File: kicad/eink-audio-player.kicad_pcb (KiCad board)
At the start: 2 copper layers, 61 x 76.1 mm, 24 parts, among them J1 Feather 16-pin, J10 TLV MICBIAS..MIC, J2 Feather 12-pin, J4 EYESPI 1-9 (5613 JP2), J5 EYESPI 10-18 (5613 JP1), J9 TLV VIN..SPKP, SW1 Power (MSK-12C03)

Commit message: High-detail Adafruit board models, ANO thumb encoder and its stand mount
Board models are Adafruit's CAD parts on Adafruit's own Eagle boards imported
into KiCad (black mask, silkscreen, ENIG pads); kicad/3d/adafruit-hq rebuilds
them. The ANO rotary encoder (6310) sits on a new printed ano_mount past the
right end of the keys, and in the KiCad design as a reference part. Renders,
anatomy and docs regenerated.

Co-Authored-By: Claude Opus 5.5 (1M context) <noreply@anthropic.com>
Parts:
- added ANO1: ANO rotary encoder (6310), stand-mounted, reference, , B.Cu at (66.7, 172.7)

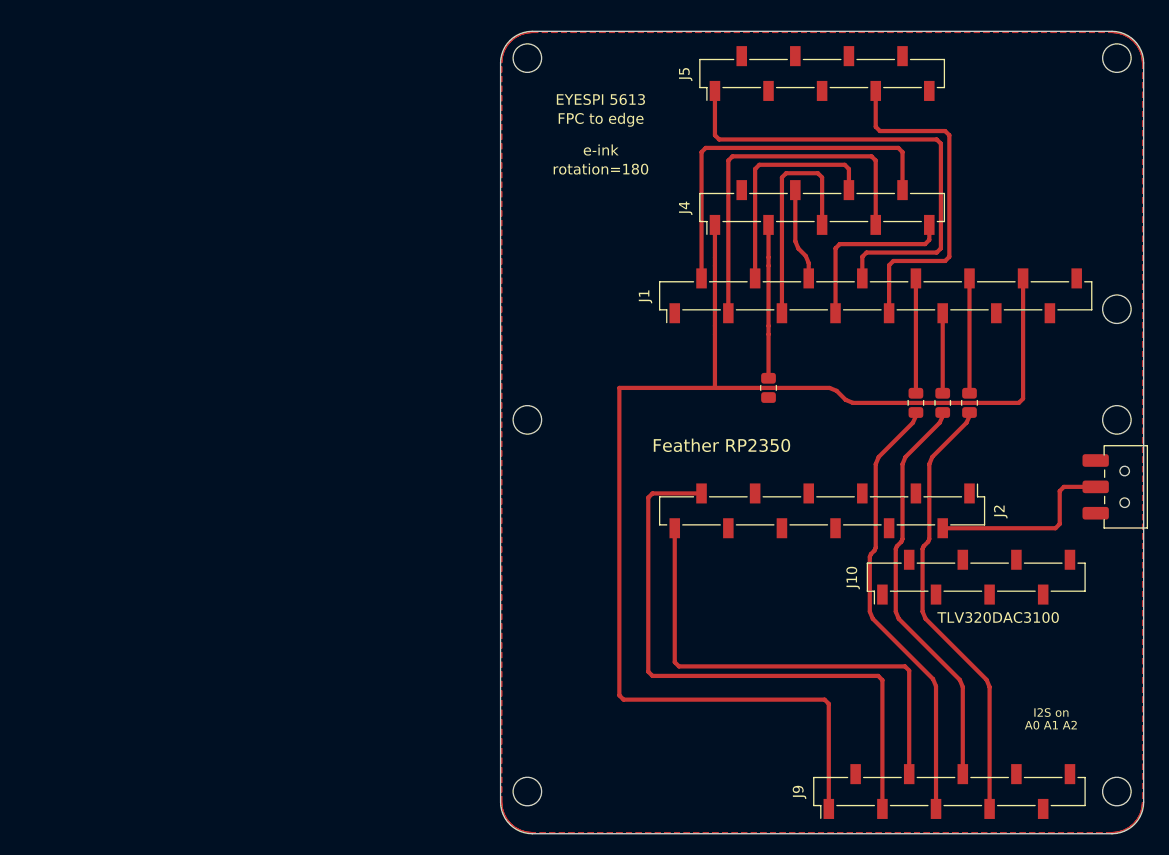
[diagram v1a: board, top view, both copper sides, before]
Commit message: Rotate the board 90 degrees to landscape (76 x 61 mm)
Drawing only; the board sits on the stand as before.

Co-Authored-By: Claude Opus 5.5 (1M context) <noreply@anthropic.com>
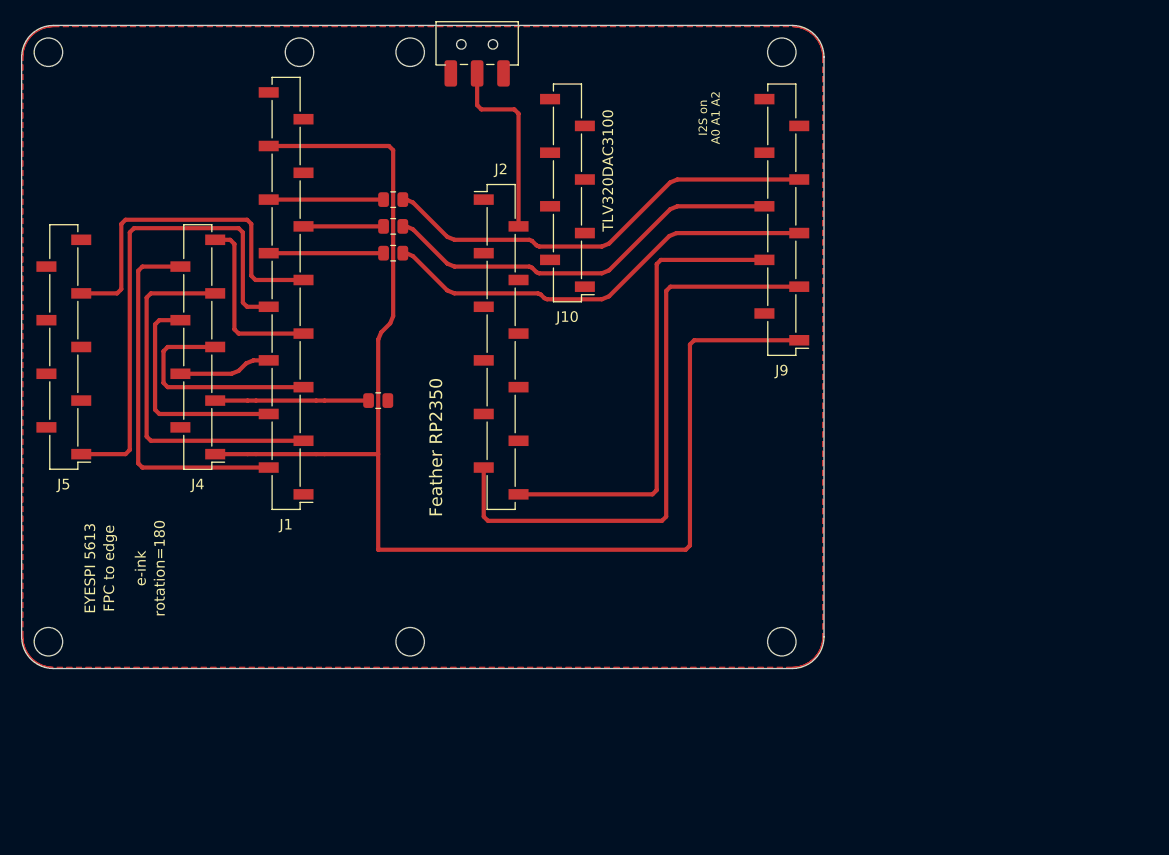
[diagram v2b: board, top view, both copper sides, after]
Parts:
- moved H2 101.3 mm to (57.1, 80.1), turned to 90 degrees
- moved A7 88.5 mm to (56.1, 95.3), turned to -90 degrees
- moved A1 86.1 mm to (78.4, 77.5), turned to -90 degrees
- moved ANO1 82.5 mm to (149.2, 171.8), turned to 90 degrees
- moved H5 81.2 mm to (80.9, 80.1), turned to 90 degrees
- moved H6 76.9 mm to (126.7, 80.1), turned to 90 degrees
- moved J5 76.4 mm to (58.6, 108.0), turned to 180 degrees
- moved H4 75.5 mm to (91.4, 80.1), turned to 90 degrees
- moved SW1 74.0 mm to (97.8, 79.6), turned to 180 degrees
- moved H1 71.6 mm to (57.1, 136.0), turned to 90 degrees
- moved J4 60.6 mm to (71.3, 108.0), turned to 180 degrees
- moved R3 57.9 mm to (89.8, 94.0), turned to 180 degrees
- moved DS1 57.1 mm to (74.3, 108.0), turned to -90 degrees
- moved J9 56.5 mm to (126.7, 96.0), turned to 180 degrees
- moved J1 55.9 mm to (79.7, 102.9), turned to 180 degrees
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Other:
- board size 61 x 76.1 mm -> 76.1 x 61 mm

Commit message: Add TP1-TP2 jumper pads for a D5 to TLV MCLK wire
Two 3.8 x 2.0 mm SMD pads: TP1 on Feather D5, TP2 on TLV320 MCLK, with
silkscreen and a schematic note. A 15 MHz PWM clock on D5 lets the TLV
PLL lock; running it from BCLK sounds muffled. DRC: no new errors.

Co-Authored-By: Claude Opus 5.5 (1M context) <noreply@anthropic.com>
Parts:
- added TP1: JUMPER, eink-audio-player:JumperPad_3.8x2.0mm, F.Cu at (107.6, 116.9)
- added TP2: JUMPER, eink-audio-player:JumperPad_3.8x2.0mm, F.Cu at (120.0, 89.9)
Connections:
- J2 pad 10: unconnected-(J2-Pin_10-Pad10) -> /D5_MCLK_JMP
- J9 pad 8: unconnected-(J9-Pin_8-Pad8) -> /MCLK
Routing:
- net /D5_MCLK_JMP: track 0.00 -> 5.90 mm
- net /MCLK: track 0.00 -> 5.13 mm
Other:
- board text added: "JMP D5>MCLK"
- board text added: "JMP MCLK<D5"
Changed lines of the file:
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@@
 			(size 1.9 1)
 			(layers "F.Cu" "F.Mask" "F.Paste")
-			(net "unconnected-(J9-Pin_8-Pad8)")
+			(net "/MCLK")
 		)
 		(pad "9" smd rect
@@
 		)
 	)
+	(footprint "eink-audio-player:JumperPad_3.8x2.0mm"
+		(layer "F.Cu")
+		(at 120 89.91)
+		(descr "Fat SMD pad for a hand-soldered jumper wire, no drill")
+		(property "Reference" "TP2"
+			(at 0 0 0)
+			(layer "F.SilkS")
+			(hide yes)
+			(effects
+				(font
+					(size 1.27 1.27)
+				)
+			)
+		)
+		(property "Value" "JUMPER"
+			(at 0 0 0)
+			(layer "F.Fab")
+			(hide yes)
+			(effects
+				(font
+					(size 1.27 1.27)
+				)
+			)
+		)
+		(property "Datasheet" ""
+			(at 0 0 0)
+			(layer "F.Fab")
+			(hide yes)
+			(effects
+				(font
+					(size 1.27 1.27)
+				)
+			)
+		)
+		(property "Description" ""
+			(at 0 0 0)
+			(layer "F.Fab")
+			(hide yes)
+			(effects
+				(font
+					(size 1.27 1.27)
+				)
+			)
+		)
+		(attr smd exclude_from_bom)
+		(duplicate_pad_numbers_are_jumpers no)
+		(fp_rect
+			(start -2.15 -1.25)
+			(end 2.15 1.25)
+			(stroke
+				(width 0.05)
+				(type default)
+			)
+			(fill no)
+			(layer "F.CrtYd")
+		)
+		(pad "1" smd roundrect
+			(at 0 0)
+			(size 3.8 2)
+			(layers "F.Cu" "F.Mask")
+			(roundrect_rratio 0.15)
+			(net "/MCLK")
+			(thermal_bridge_angle 45)
+		)
+		(embedded_fonts no)
+	)
 	(footprint "eink-audio-player:SW_SPDT_MSK-12C03"
 		(layer "F.Cu")
@@
 		)
 	)
+	(footprint "eink-audio-player:JumperPad_3.8x2.0mm"
+		(layer "F.Cu")
+		(at 107.6 116.91)
+		(descr "Fat SMD pad for a hand-soldered jumper wire, no drill")
+		(property "Reference" "TP1"
+			(at 0 0 0)
+			(layer "F.SilkS")
+			(hide yes)
+			(effects
+				(font
+					(size 1.27 1.27)
+				)
+			)
+		)
+		(property "Value" "JUMPER"
+			(at 0 0 0)
+			(layer "F.Fab")
+			(hide yes)
+			(effects
+				(font
+					(size 1.27 1.27)
+				)
+			)
+		)
+		(property "Datasheet" ""
+			(at 0 0 0)
+			(layer "F.Fab")
+			(hide yes)
+			(effects
+				(font
+					(size 1.27 1.27)
+				)
+			)
+		)
+		(property "Description" ""
+			(at 0 0 0)
+			(layer "F.Fab")
+			(hide yes)
+			(effects
+				(font
+					(size 1.27 1.27)
+				)
+			)
+		)
+		(attr smd exclude_from_bom)
+		(duplicate_pad_numbers_are_jumpers no)
+		(fp_rect
+			(start -2.15 -1.25)
+			(end 2.15 1.25)
+			(stroke
+				(width 0.05)
+				(type default)
+			)
+			(fill no)
+			(layer "F.CrtYd")
+		)
+		(pad "1" smd roundrect
+			(at 0 0)
+			(size 3.8 2)
+			(layers "F.Cu" "F.Mask")
+			(roundrect_rratio 0.15)
+			(net "/D5_MCLK_JMP")
+			(thermal_bridge_angle 45)
+		)
+		(embedded_fonts no)
+	)
 	(footprint "MountingHole:MountingHole_2.7mm"
 		(layer "F.Cu")
@@
 			(size 1.9 1)
 			(layers "F.Cu" "F.Mask" "F.Paste")
-			(net "unconnected-(J2-Pin_10-Pad10)")
+			(net "/D5_MCLK_JMP")
 		)
 		(pad "11" smd rect
@@
 		)
 	)
+	(gr_text "JMP\nD5>MCLK"
+		(at 107.6 119.509999 0)
+		(layer "F.SilkS")
+		(effects
+			(font
+				(size 0.8 0.8)
+				(thickness 0.15)
+			)
+		)
+	)
+	(gr_text "JMP\nMCLK<D5"
+		(at 114.6 87.6 0)
+		(layer "F.SilkS")
+		(effects
+			(font
+				(size 0.8 0.8)
+				(thickness 0.15)
+			)
+		)
+	)
 	(gr_text "EYESPI 5613"
 		(at 61.1 129 90)
@@
 		(net "/GND_R4")
 	)
+	(segment
+		(start 101.7 116.91)
+		(end 107.6 116.91)
+		(width 0.4)
+		(layer "F.Cu")
+		(net "/D5_MCLK_JMP")
+	)
+	(segment
+		(start 125.01 89.61)
+		(end 124.71 89.91)
+		(width 0.4)
+		(layer "F.Cu")
+		(net "/MCLK")
+	)
+	(segment
+		(start 124.71 89.91)
+		(end 120 89.91)
+		(width 0.4)
+		(layer "F.Cu")
+		(net "/MCLK")
+	)
 	(zone
